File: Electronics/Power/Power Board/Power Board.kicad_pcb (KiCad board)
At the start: 4 copper layers, 65 x 85 mm, 167 parts, among them IC201 INA219AIDR, IC202 TLV1805DBVR, IC203 INA219AIDR, IC204 INA219AIDR, IC205 MP28167GQ-A-Z, IC206 TPS563202DRLR, IC207 TPS563202DRLR, IC208 TLV1805DBVR, IC301 STM32U575VGT6, IC302 TJA1057GT/3, J201 XT60PW-F, J202 Conn_01x02_Pin, J203 XT60PW-M, J204 Screw_Terminal_01x02, J206 Conn_01x02_Pin, J207 Screw_Terminal_01x02, J208 Screw_Terminal_01x02, J209 Conn_01x02_Pin, J210 Screw_Terminal_01x02, J211 Screw_Terminal_01x02, J213 Screw_Terminal_01x02, J214 Screw_Terminal_01x02, J215 Screw_Terminal_01x02, J301 TC2030, J302 TYPE-C-31-M-12, J303 Screw_Terminal_01x03, Q201 DMP3013SFV-7, Q202 DMP3013SFV-7, Q203 DMP3013SFV-7, Q204 DMP3013SFV-7, Q205 DMP3013SFV-7, Q206 SSM6K513NU,LF, Q207 SSM6K513NU,LF, SW201 SW_SPDT, SW301 SW_DIP_x02, U201 TCKE800NA_RF, U202 TCKE812NA_RF, U203 TVS1800DRV, U302 USBLC6-4SC6-ES, U303 TVS1800DRV, X301 25MHz_Clock, X302 32.768kHz_Clock

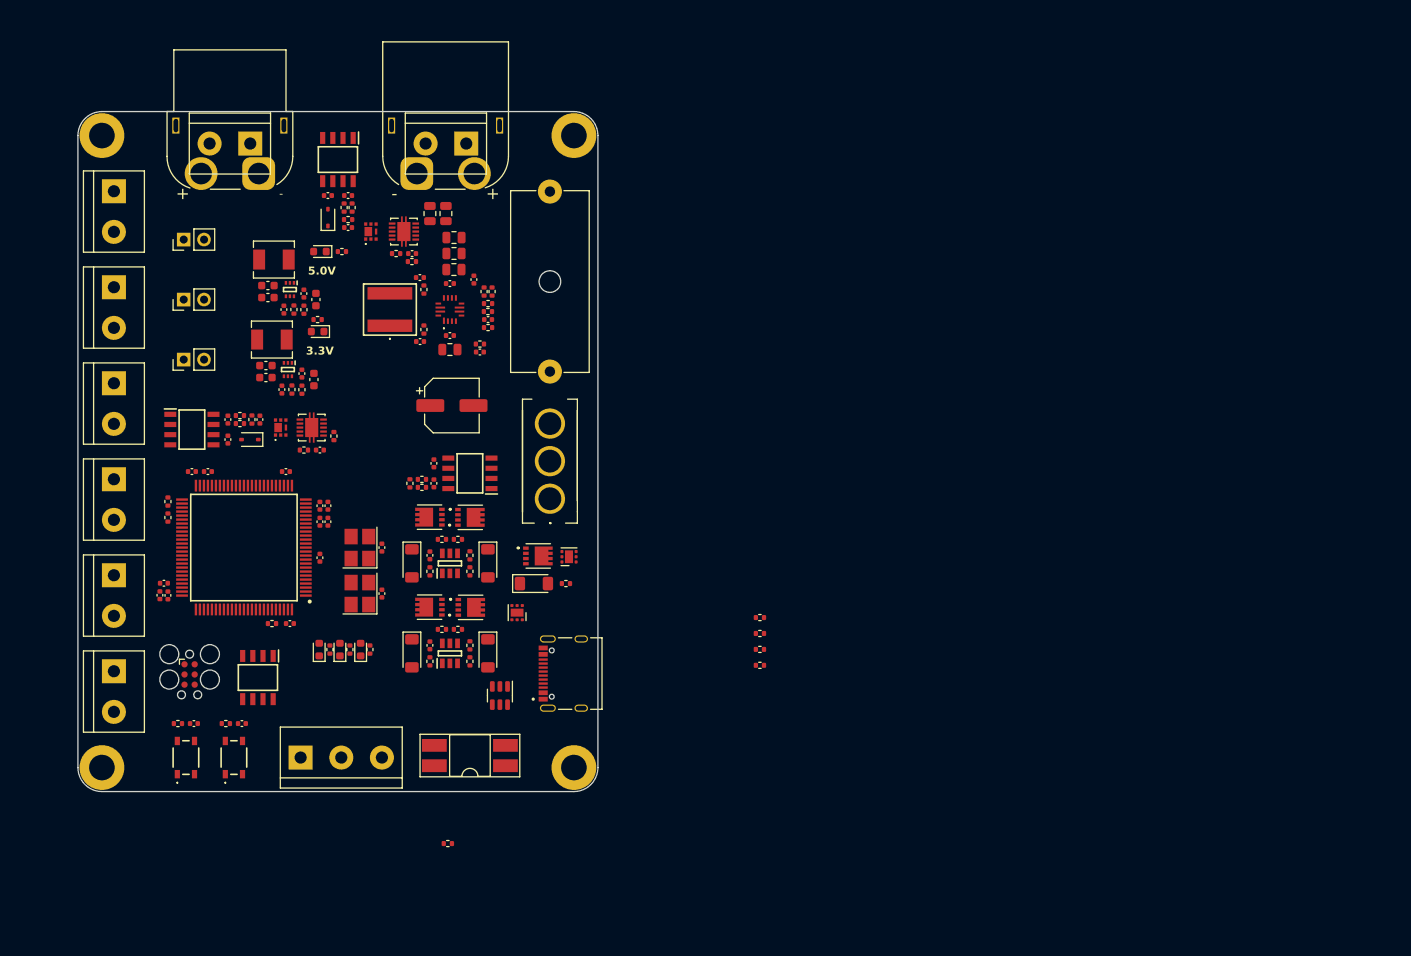
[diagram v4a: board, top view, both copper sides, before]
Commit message: Gateway board layout complete and routing begun
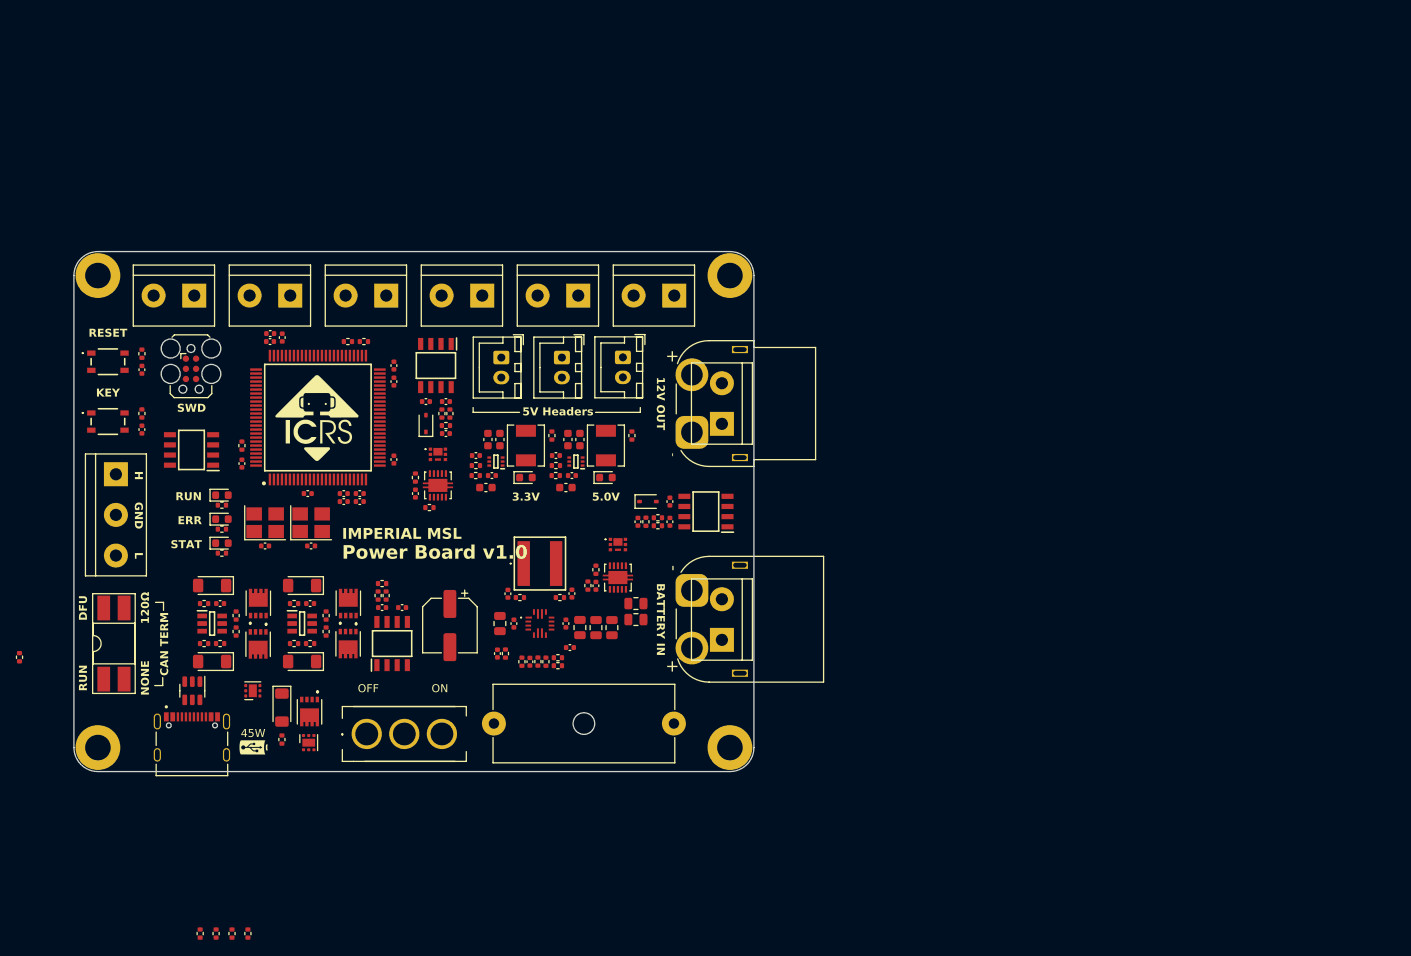
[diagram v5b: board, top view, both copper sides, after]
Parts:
- removed D207: GREEN, LED_SMD:LED_0603_1608Metric
- removed J209: Conn_01x02_Pin, Connector_PinHeader_2.54mm:PinHeader_1x02_P2.54mm_Vertical
- added D202: GREEN, LED_SMD:LED_0603_1608Metric, F.Cu at (176.0, 95.8)
- added G***: LOGO, MSL Footprints:ICRS_12mm, F.Cu at (140.0, 88.2)
- added G***: LOGO, MSL Footprints:UCPD_logo_4mm, F.Cu at (132.0, 129.4)
- added G***: LOGO, MSL Footprints:DC_logo_4mm, B.Cu at (178.4, 122.5)
- added G***: LOGO, footprints:ICRS Medium, B.Cu at (152.0, 100.0)
- added G***: LOGO, MSL Footprints:DC_logo_4mm, B.Cu at (179.0, 95.5)
- added J205: JST-XH-2.50mm, Connector_JST:JST_XH_B2B-XH-A_1x02_P2.50mm_Vertical, F.Cu at (162.9, 80.8)
- added REF**: ESD-Logo_8.9x8mm_SilkScreen, Symbol:ESD-Logo_8.9x8mm_SilkScreen, B.Cu at (130.3, 115.8)
- added REF**: WEEE-Logo_5.6x8mm_SilkScreen, Symbol:WEEE-Logo_5.6x8mm_SilkScreen, B.Cu at (119.7, 115.6)
- J202, J206: value Conn_01x02_Pin -> JST-XH-2.50mm; footprint Connector_PinHeader_2.54mm:PinHeader_1x02_P2.54mm_Vertical -> Connector_JST:JST_XH_B2B-XH-A_1x02_P2.50mm_Vertical
- J207, J208, J210, J211, J213, J214: value Screw_Terminal_01x02 -> Pluggable_Terminal_01x02; footprint TerminalBlock:TerminalBlock_bornier-2_P5.08mm -> MSL Footprints:Pluggable_terminal-2_P5.08mm
- J301: footprint Connector:Tag-Connect_TC2030-IDC-FP_2x03_P1.27mm_Vertical -> MSL Footprints:Tag-Connect_TC2030-IDC-FP_2x03_P1.27mm_Vertical
- J303: value Screw_Terminal_01x03 -> Pluggable_Terminal_01x03; footprint TerminalBlock:TerminalBlock_bornier-3_P5.08mm -> MSL Footprints:Pluggable_terminal-3_P5.08mm
- R210: value 330R -> 4k7
- moved H101 80.4 mm to (191.5, 70.5), turned to -90 degrees
- moved H103 78.9 mm to (191.5, 129.5), turned to -90 degrees
- moved R313 77.6 mm to (125.3, 152.8), turned to -90 degrees
- moved R312 76.7 mm to (127.3, 152.8), turned to -90 degrees
- moved R311 75.9 mm to (129.3, 152.8), turned to -90 degrees
- moved R310 75.2 mm to (131.2, 152.8), turned to -90 degrees
- moved J213 71.2 mm to (184.5, 73.0), turned to 180 degrees
- moved J204 69.8 mm to (190.5, 116.0), turned to 90 degrees
- moved J215 68.6 mm to (190.5, 89.0), turned to 90 degrees
- moved F201 68.3 mm to (184.5, 126.5), turned to 180 degrees
- moved IC201 63.7 mm to (188.5, 100.0), turned to 180 degrees
- moved J201 63.1 mm to (186.8, 90.1), turned to -90 degrees
- moved J203 62.4 mm to (186.8, 109.9), turned to -90 degrees
- moved H102 61.5 mm to (112.5, 70.5), turned to -90 degrees
- moved H104 59.6 mm to (112.5, 129.5), turned to -90 degrees
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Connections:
- D206 pad 1: /Power/5V_LED_K -> GND
- D206 pad 2: +5V -> /Power/3V3_LED_A
- R228 pad 1: /Power/5V_LED_K -> +5V
- R228 pad 2: GND -> /Power/5V_LED_A
- R229 pad 1: /Power/3V3_LED_K -> +3.3V
- R229 pad 2: GND -> /Power/3V3_LED_A
- SW301 pad 1: /Control/CAN_SW -> +3V3
- SW301 pad 2: +3V3 -> /Control/CAN_SW
- SW301 pad 3: BOOT0 -> /Control/CANH
- SW301 pad 4: /Control/CANH -> BOOT0
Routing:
- added copper zone on In1.Cu, net GND
- added copper zone on In2.Cu, net GND
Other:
- board size 65 x 85 mm -> 85 x 65 mm
- board text added: "+"
- board text added: "-"
- board text added: "120Ω"
- board text added: "12V OUT"
- board text added: "45W"
- board text added: "5-16V DC"
- board text added: "5V"
- board text added: "5V Headers"
- board text added: "BATTERY IN"
- board text added: "CAN TERM"
- board text added: "DFU"
- board text added: "Designed by Ben Smith 2023"
- board text added: "ERR"
- board text added: "FD-CAN"
- board text added: "GND"
- board text added: "H"
- board text added: "Input: 5-16V 5A"
- board text added: "KEY"
- board text added: "L"
- board text added: "NONE"
- board text added: "OFF"
- board text added: "ON"
- board text added: "Output: 12V 3A"
- board text added: "RESET"
- board text added: "RUN"
- board text added: "STAT"
- board text added: "SWD"
- board text added: "_{IMPERIAL MSL} Power Board v1.0"

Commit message: Sensor hub board done
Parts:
- removed REF**: ESD-Logo_8.9x8mm_SilkScreen, Symbol:ESD-Logo_8.9x8mm_SilkScreen
- removed REF**: WEEE-Logo_5.6x8mm_SilkScreen, Symbol:WEEE-Logo_5.6x8mm_SilkScreen
- added G***: LOGO, MSL Footprints:DC_logo_4mm, B.Cu at (144.0, 69.4)
- moved R301 15.8 mm to (118.5, 116.5)
- moved C233 1.82 mm to (174.3, 107.5)
- moved Q207 1.82 mm to (177.0, 102.4)
- moved R209 1.82 mm to (173.2, 107.5)
- moved R212 1.82 mm to (174.3, 105.5)
- moved U202 1.82 mm to (177.0, 106.5)
- moved C222 1.74 mm to (179.4, 109.8)
- moved C226 1.74 mm to (179.4, 111.8)
- moved U303 0.91 mm to (131.1, 122.8)
- moved J301 0.70 mm to (124.0, 82.8)
- moved R305 0.55 mm to (146.3, 78.8)
- moved C301 0.50 mm to (133.9, 104.3)
- moved C302 0.50 mm to (139.7, 104.3)
- moved R306 0.45 mm to (144.2, 78.8)
- moved C309 0.40 mm to (149.9, 83.8)
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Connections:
- C202 pad 2: +3V3 -> +3.3V
- C206 pad 2: +3V3 -> +3.3V
- C236 pad 2: +3V3 -> +3.3V
- C301 pad 1: +3V3 -> +3.3V
- C302 pad 2: +3V3 -> +3.3V
- C307 pad 1: +3V3 -> +3.3V
- C308 pad 1: +3V3 -> +3.3V
- C310 pad 1: +3V3 -> +3.3V
- C311 pad 1: +3V3 -> +3.3V
- C312 pad 1: +3V3 -> +3.3V
- C313 pad 1: +3V3 -> +3.3V
- C314 pad 1: +3V3 -> +3.3V
- C315 pad 1: +3V3 -> +3.3V
- C316 pad 1: +3V3 -> +3.3V
- IC201 pad 2: +3V3 -> +3.3V
- IC201 pad 5: +3V3 -> +3.3V
- IC203 pad 5: +3V3 -> +3.3V
- IC204 pad 5: +3V3 -> +3.3V
- IC301 pad 100: +3V3 -> +3.3V
- IC301 pad 11: +3V3 -> +3.3V
- IC301 pad 22: +3V3 -> +3.3V
- IC301 pad 28: +3V3 -> +3.3V
- IC301 pad 50: +3V3 -> +3.3V
- IC301 pad 6: +3V3 -> +3.3V
- IC301 pad 73: +3V3 -> +3.3V
- IC301 pad 75: +3V3 -> +3.3V
- IC302 pad 5: +3V3 -> +3.3V
- J301 pad 1: +3V3 -> +3.3V
- R302 pad 2: +3V3 -> +3.3V
- R303 pad 2: +3V3 -> +3.3V
- R305 pad 1: +3V3 -> +3.3V
- R306 pad 1: +3V3 -> +3.3V
- SW301 pad 1: +3V3 -> +3.3V
- U302 pad 1: /Control/CC1 -> /Control/CC2
- U302 pad 3: /Control/CC2 -> /Control/CC1
- U302 pad 4: USB_DP -> USB_DN
- U302 pad 5: +3V3 -> +3.3V
- U302 pad 6: USB_DN -> USB_DP
- X301 pad 4: +3V3 -> +3.3V
- X302 pad 4: +3V3 -> +3.3V
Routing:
- net GND: track 0.00 -> 82.4 mm, vias 0 -> 52
- net SCL: track 0.00 -> 67.1 mm, vias 0 -> 2
- net SDA: track 0.00 -> 66.7 mm, vias 0 -> 2
- net USB_DP: track 0.00 -> 65.2 mm, vias 0 -> 2
- net USB_DN: track 0.00 -> 64.5 mm, vias 0 -> 2
- net +3.3V: track 0.00 -> 48.0 mm, vias 0 -> 18
- net +5V: track 0.00 -> 40.7 mm, vias 0 -> 1
- net NRST: track 0.00 -> 39.8 mm, vias 0 -> 2
- net /Control/CANL: track 0.00 -> 37.4 mm
- net /Control/CANH: track 0.00 -> 26.4 mm
- net SWDIO: track 0.00 -> 15.3 mm
- net CAN_TX: track 0.00 -> 12.5 mm
- net SWO: track 0.00 -> 9.54 mm, vias 0 -> 2
- net CAN_RX: track 0.00 -> 9.46 mm
- net /Power/VBUS_GATE: track 0.00 -> 9.14 mm
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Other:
- board text added: "Output: Battery voltage 3A total"
- board text added: "locked"

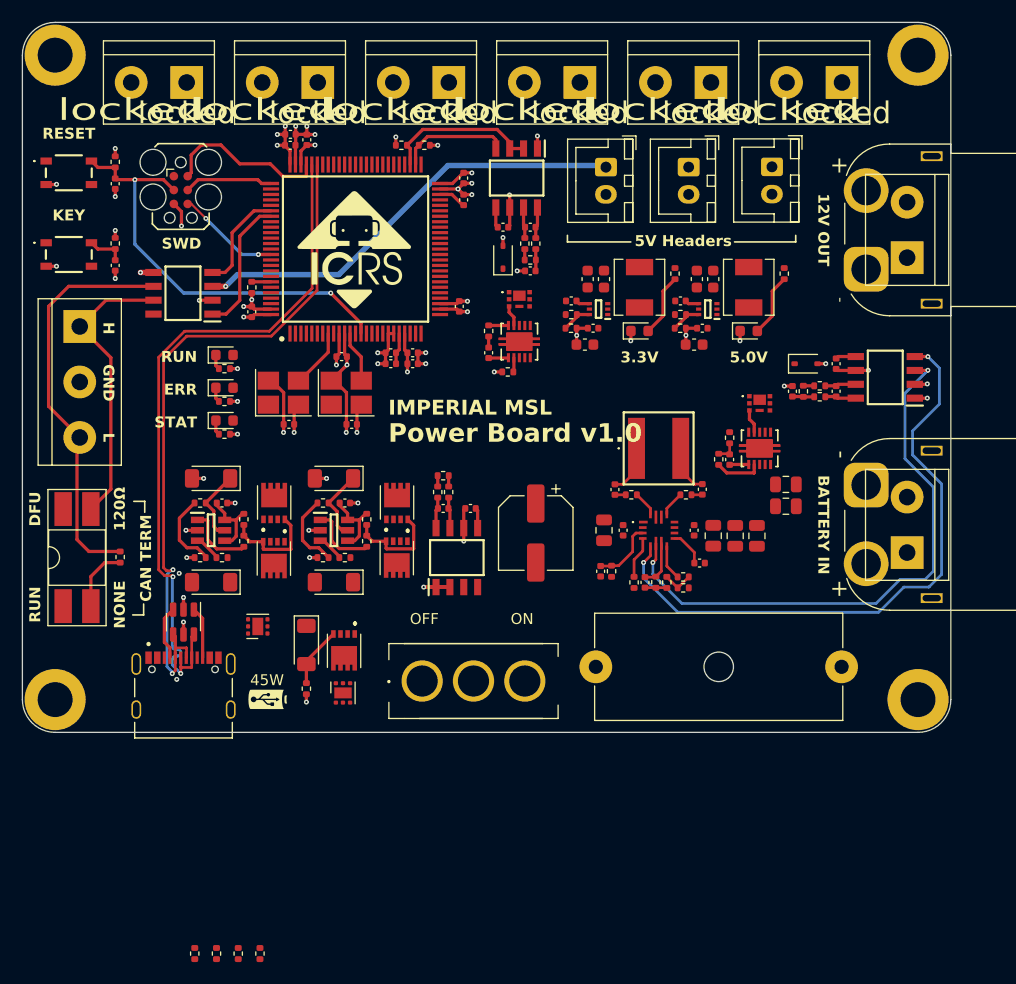
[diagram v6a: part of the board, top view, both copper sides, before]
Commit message: Motor driver and power boards done
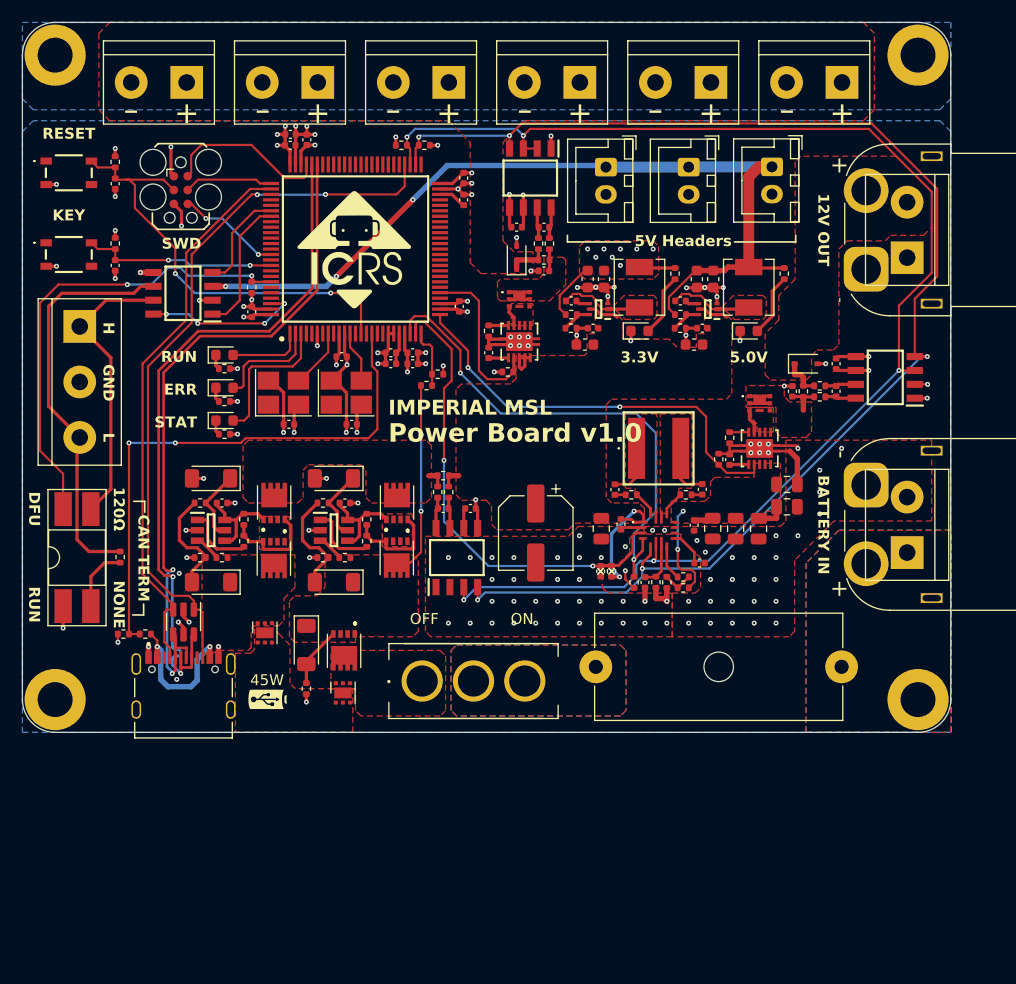
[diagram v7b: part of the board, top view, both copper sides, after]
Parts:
- added REF**: WEEE-Logo_5.6x8mm_SilkScreen, Symbol:WEEE-Logo_5.6x8mm_SilkScreen, B.Cu at (130.4, 118.2)
- added REF**: ESD-Logo_8.9x8mm_SilkScreen, Symbol:ESD-Logo_8.9x8mm_SilkScreen, B.Cu at (120.7, 118.2)
- R202, R214: value 10m -> 2m
- moved R311 56.1 mm to (147.5, 99.7), turned to 0 degrees
- moved R310 54.2 mm to (146.5, 100.8), turned to 0 degrees
- moved R313 30.0 mm to (118.8, 123.5), turned to 180 degrees
- moved R312 30.0 mm to (120.8, 123.5), turned to 180 degrees
- moved C235 1.25 mm to (157.2, 86.2)
- moved C236 1.25 mm to (154.8, 86.2)
- moved C238 1.25 mm to (157.2, 90.2)
- moved D210 1.25 mm to (154.8, 89.0)
- moved IC203 1.25 mm to (156.0, 81.8)
- moved R236 1.25 mm to (157.8, 87.8)
- moved R237 1.25 mm to (157.2, 89.2)
- moved R238 1.25 mm to (156.8, 87.8)
- moved U303 0.88 mm to (131.7, 123.4), turned to 90 degrees
- moved C227 0.68 mm to (176.9, 113.8)
- moved C223 0.66 mm to (172.7, 113.8)
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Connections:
- IC301 pad 1: unconnected-(IC301-PE2-Pad1) -> LEDG
- IC301 pad 16: unconnected-(IC301-PC1-Pad16) -> VBUS/11
- IC301 pad 2: unconnected-(IC301-PE3-Pad2) -> LEDR
- IC301 pad 23: unconnected-(IC301-PA0-Pad23) -> ALT
- IC301 pad 24: unconnected-(IC301-PA1-Pad24) -> 12V_EN
- IC301 pad 25: unconnected-(IC301-PA2-Pad25) -> VBAT/11
- IC301 pad 26: unconnected-(IC301-PA3-Pad26) -> 12V_OUT_EN
- IC301 pad 3: unconnected-(IC301-PE4-Pad3) -> LEDB
- IC301 pad 30: unconnected-(IC301-PA5-Pad30) -> VOUT_EN
- IC301 pad 91: unconnected-(IC301-PB5-Pad91) -> BTN
- IC301 pad 98: unconnected-(IC301-PE1-Pad98) -> SILENT
- J302 pad S2: unconnected-(J302-SHIELD-PadS1) -> unconnected-(J302-SHIELD-PadS2)
- J302 pad S3: unconnected-(J302-SHIELD-PadS1) -> unconnected-(J302-SHIELD-PadS3)
- J302 pad S4: unconnected-(J302-SHIELD-PadS1) -> unconnected-(J302-SHIELD-PadS4)
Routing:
- net /Control/CC2: track 4.73 -> 65.9 mm, vias 0 -> 2
- net SDA: track 66.7 -> 127.3 mm, vias 2 -> 5
- net SCL: track 67.1 -> 126.0 mm, vias 2 -> 5
- net VBUS/11: track 0.00 -> 50.7 mm, vias 0 -> 2
- net /Control/CC1: track 4.94 -> 50.9 mm
- net ALT: track 3.84 -> 45.8 mm, vias 0 -> 2
- net BOOT0: track 1.76 -> 43.1 mm, vias 0 -> 2
- net +5V: track 40.7 -> 80.2 mm, vias 1 -> 3
- net 12V_EN: track 5.93 -> 43.4 mm, vias 0 -> 2
- net GND: track 82.4 -> 117.0 mm, vias 52 -> 135
- net 12V_OUT_EN: track 4.32 -> 38.8 mm, vias 0 -> 2
- net VDD: track 0.99 -> 22.6 mm, vias 0 -> 2
- net +3.3V: track 48.0 -> 68.0 mm, vias 18 -> 33
- net VBAT: track 0.00 -> 17.9 mm, vias 0 -> 2
- net BTN: track 3.43 -> 17.9 mm, vias 0 -> 2
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- added copper zone on F.Cu, net +12V
- added copper zone on B.Cu, net +3.3V
- added copper zone on F.Cu, net +3.3V
- added copper zone on F.Cu, net /Power/12V_OUT
- added copper zone on F.Cu, net /Power/12V_OUT_D
- added copper zone on F.Cu, net /Power/12V_OUT_S
- added copper zone on F.Cu, net /Power/12V_SW1
- added copper zone on F.Cu, net /Power/12V_SW2
- added copper zone on F.Cu, net /Power/3V3_SW
- added copper zone on F.Cu, net /Power/5V_SW
- added copper zone on B.Cu, net /Power/VBAT_FUSED
- added copper zone on F.Cu, net /Power/VBAT_FUSED
- added copper zone on F.Cu, net /Power/VBAT_SOURCE
- added copper zone on F.Cu, net /Power/VBAT_SWITCHED
- added copper zone on F.Cu, net /Power/VBUS_SOURCE
- added copper zone on F.Cu, net /Power/VOUT_D
- added copper zone on F.Cu, net /Power/VOUT_S
- added copper zone on F.Cu, net GND
- added copper zone on F.Cu, net VBAT
- added copper zone on B.Cu, net VBAT_RAW
- added copper zone on F.Cu, net VBAT_RAW
- added copper zone on F.Cu, net VBUS
- added copper zone on F.Cu, net VDD
- added copper zone on F.Cu, net VIN
- added copper zone on B.Cu, net VOUT
- added copper zone on F.Cu, net VOUT
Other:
- board text added: "Input: 5-16V 6A"
- board text removed: "5-16V DC"
- board text removed: "Input: 5-16V 5A"
- board text removed: "locked"

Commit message: All boards done
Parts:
- moved REF** 0.36 mm to (121.0, 118.0)
- moved REF** 0.36 mm to (130.7, 118.0)
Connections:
- H101 pad 1: GND -> unconnected-(H101-Pad1)
- H102 pad 1: GND -> unconnected-(H102-Pad1)
- H103 pad 1: GND -> unconnected-(H103-Pad1)
- H104 pad 1: GND -> unconnected-(H104-Pad1)
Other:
- board text added: "locked"
- board text removed: "+"
- board text removed: "-"
- board text removed: "120Ω"
- board text removed: "12V OUT"
- board text removed: "3.3V"
- board text removed: "45W"
- board text removed: "5.0V"
- board text removed: "5V"
- board text removed: "5V Headers"
- board text removed: "BATTERY IN"
- board text removed: "CAN TERM"
- board text removed: "DFU"
- board text removed: "Designed by Ben Smith 2023"
- board text removed: "ERR"
- board text removed: "FD-CAN"
- board text removed: "GND"
- board text removed: "H"
- board text removed: "Input: 5-16V 6A"
- board text removed: "KEY"
- board text removed: "L"
- board text removed: "NONE"
- board text removed: "OFF"
- board text removed: "ON"
- board text removed: "Output: 12V 3A"
- board text removed: "Output: Battery voltage 3A total"
- board text removed: "RESET"
- board text removed: "RUN"
- board text removed: "STAT"
- board text removed: "SWD"
- board text removed: "_{IMPERIAL MSL} Power Board v1.0"
